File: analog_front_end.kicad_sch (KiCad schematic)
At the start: 14 parts, among them J3 Conn_01x03_Pin, J4 Conn_01x03_Pin, Q3 BC847,215, Q4 BSS316N, U7 OPA388IDBV

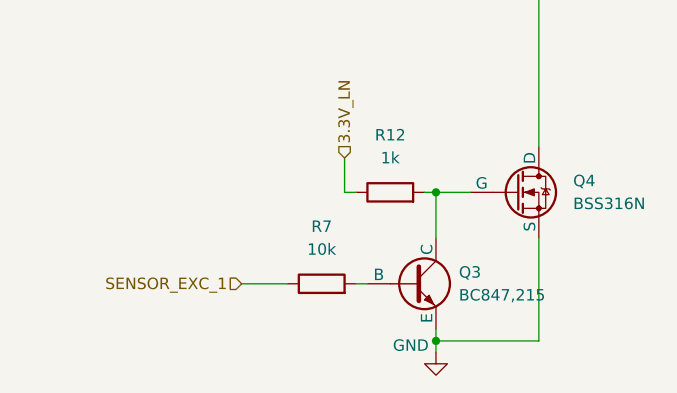
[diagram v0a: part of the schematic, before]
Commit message: rule-check: Fix the ERC errors and warnings
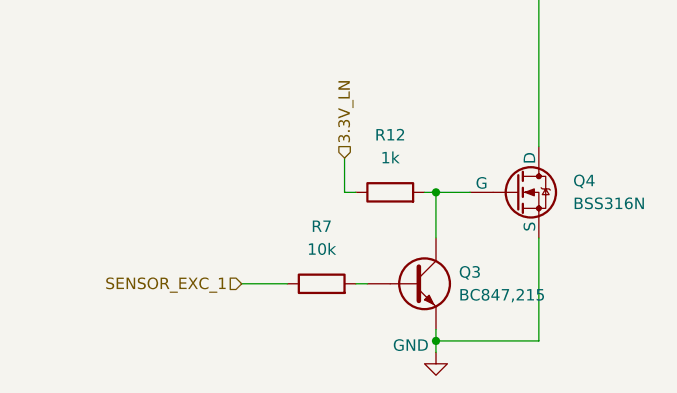
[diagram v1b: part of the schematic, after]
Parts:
- Q3: symbol Simulation_SPICE:NPN -> Device:Q_NPN
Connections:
- net GND: now also Q3.E; no longer Q3.3 (E)
- net at R7.2: now also Q3.B; no longer Q3.2 (B)
- net at Q4.2 (G), R12.2: now also Q3.C; no longer Q3.1 (C)
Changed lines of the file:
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@@
+			)
+		)
+		(property "LCSC" ""
+			(at 86.36 111.76 0)
+			(effects
+				(font
+					(size 1.27 1.27)
+				)
+				(hide yes)
 			)
 		)
@@
 	)
 	(symbol
-		(lib_id "Simulation_SPICE:NPN")
+		(lib_id "Device:Q_NPN")
 		(at 193.04 140.97 0)
 		(unit 1)
@@
 			)
 		)
-		(pin "2"
-		)
-		(pin "1"
-		)
-		(pin "3"
-		)
-		(instances
+		(property "LCSC" ""
+			(at 193.04 140.97 0)
+			(effects
+				(font
+					(size 1.27 1.27)
+				)
+				(hide yes)
+			)
+		)
+		(pin "C"
+		)
+		(pin "B"
+		)
+		(pin "E"
+		)
+		(instances

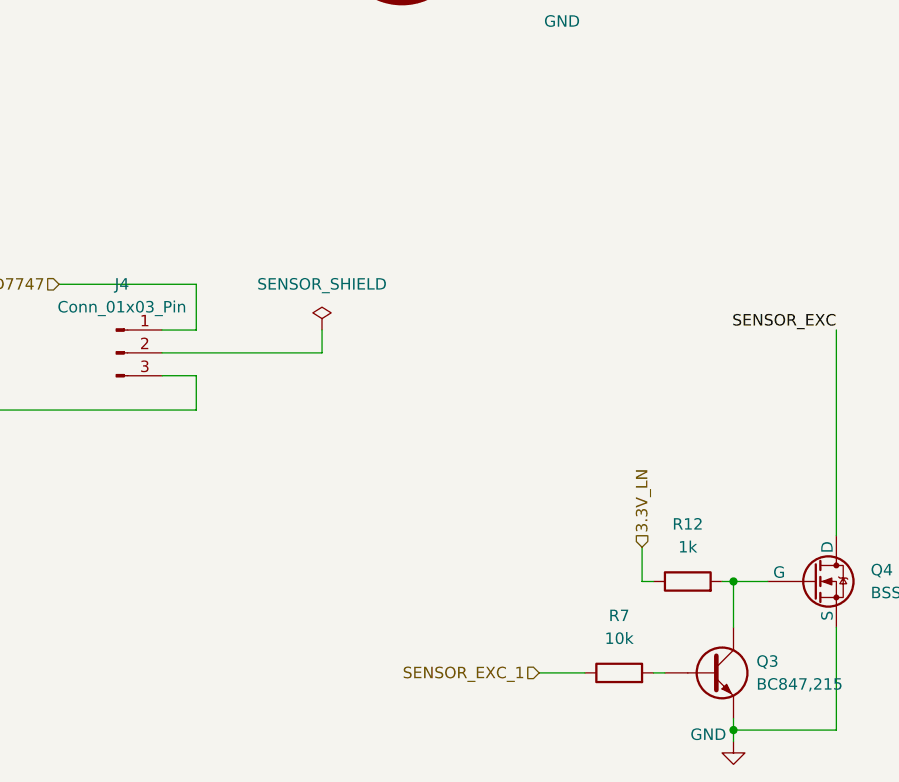
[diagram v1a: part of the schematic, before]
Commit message: design: fix some rules check
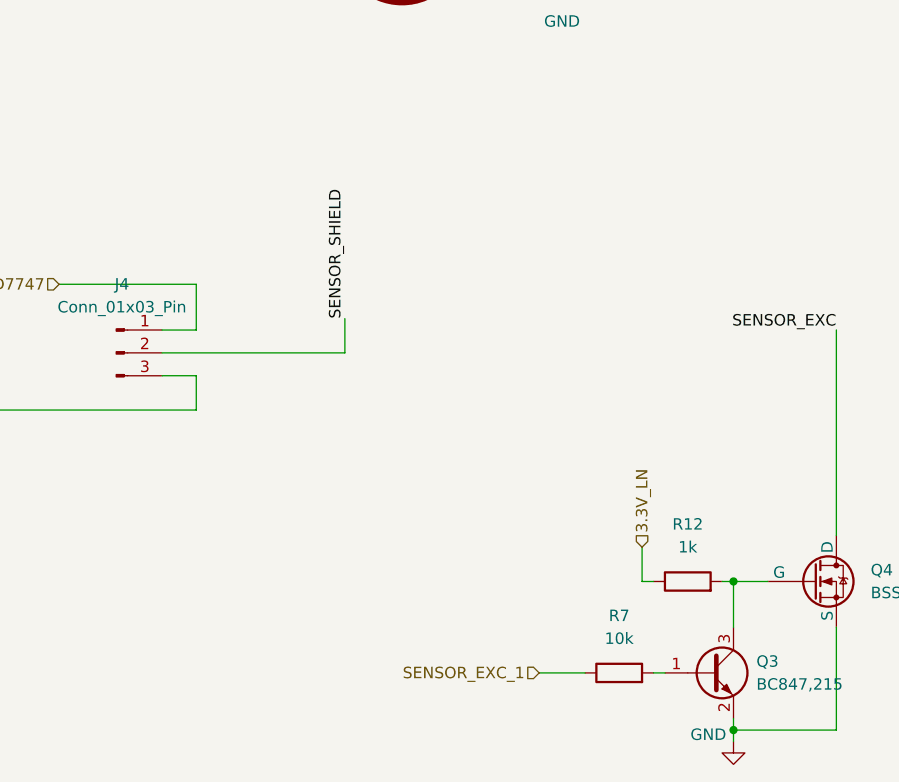
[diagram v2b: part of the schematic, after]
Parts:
- Q3: symbol Device:Q_NPN -> Transistor_BJT:BC847
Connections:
- net GND: now also Q3.2 (E); no longer Q3.E
- net at R7.2: now also Q3.1 (B); no longer Q3.B
- net at Q4.2 (G), R12.2: now also Q3.3 (C); no longer Q3.C
- net SENSOR_SHIELD: now reaches J4.2 (Pin_2)
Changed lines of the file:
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@@
 	(wire
 		(pts
-			(xy 149.86 102.87) (xy 149.86 105.41)
+			(xy 152.4 101.6) (xy 152.4 105.41)
 		)
 		(stroke
@@
 	(wire
 		(pts
-			(xy 132.08 105.41) (xy 149.86 105.41)
+			(xy 132.08 105.41) (xy 152.4 105.41)
 		)
 		(stroke
@@
 			(width 0)
 			(type default)
+		)
+	)
+	(label "SENSOR_SHIELD"
+		(at 152.4 101.6 90)
+		(effects
+			(font
+				(size 1.27 1.27)
+			)
+			(justify left bottom)
 		)
 	)
@@
 	)
 	(symbol
-		(lib_id "power:PWR_FLAG")
-		(at 149.86 102.87 0)
-		(unit 1)
-		(exclude_from_sim no)
-		(in_bom yes)
-		(on_board yes)
-		(dnp no)
-		(fields_autoplaced yes)
-		(property "Reference" "#FLG01"
-			(at 149.86 100.965 0)
-			(effects
-				(font
-					(size 1.27 1.27)
-				)
-				(hide yes)
-			)
-		)
-		(property "Value" "SENSOR_SHIELD"
-			(at 149.86 97.79 0)
-			(effects
-				(font
-					(size 1.27 1.27)
-				)
-			)
-		)
-		(property "Footprint" ""
-			(at 149.86 102.87 0)
-			(effects
-				(font
-					(size 1.27 1.27)
-				)
-				(hide yes)
-			)
-		)
-		(property "Datasheet" "~"
-			(at 149.86 102.87 0)
-			(effects
-				(font
-					(size 1.27 1.27)
-				)
-				(hide yes)
-			)
-		)
-		(property "Description" "Special symbol for telling ERC where power comes from"
-			(at 149.86 102.87 0)
-			(effects
-				(font
-					(size 1.27 1.27)
-				)
-				(hide yes)
-			)
-		)
-		(pin "1"
-		)
-		(instances
-			(project ""
-				(path "/dedd74c5-8e82-403a-8a1b-f763d3ee00bb/2a3fb7ae-12df-4167-9b5f-4fb9d4c182aa"
-					(reference "#FLG01")
-					(unit 1)
-				)
-			)
-		)
-	)
-	(symbol
 		(lib_id "Connector:Conn_01x03_Pin")
 		(at 115.57 59.69 0)
@@
 	)
 	(symbol
-		(lib_id "Device:Q_NPN")
+		(lib_id "Transistor_BJT:BC847")
 		(at 193.04 140.97 0)
 		(unit 1)
@@
 		)
 		(property "Footprint" "Package_TO_SOT_SMD:SOT-23"
-			(at 256.54 140.97 0)
-			(effects
-				(font
-					(size 1.27 1.27)
-				)
-				(hide yes)
-			)
-		)
-		(property "Datasheet" "https://ngspice.sourceforge.io/docs/ngspice-html-manual/manual.xhtml#cha_BJTs"
-			(at 256.54 140.97 0)
-			(effects
-				(font
-					(size 1.27 1.27)
-				)
-				(hide yes)
-			)
-		)
-		(property "Description" "Bipolar transistor symbol for simulation only, substrate tied to the emitter"
+			(at 198.12 142.875 0)
+			(effects
+				(font
+					(size 1.27 1.27)
+					(italic yes)
+				)
+				(justify left)
+				(hide yes)
+			)
+		)
+		(property "Datasheet" "http://www.infineon.com/dgdl/Infineon-BC847SERIES_BC848SERIES_BC849SERIES_BC850SERIES-DS-v01_01-en.pdf?fileId=db3a304314dca389011541d4630a1657"
+			(at 193.04 140.97 0)
+			(effects
+				(font
+					(size 1.27 1.27)
+				)
+				(justify left)
+				(hide yes)
+			)
+		)
+		(property "Description" "0.1A Ic, 45V Vce, NPN Transistor, SOT-23"
 			(at 193.04 140.97 0)
 			(effects
@@
 			)
 		)
-		(property "Sim.Pins" "1=C 2=B 3=E"
+		(property "Sim.Pins" "C=C B=B E=E"
 			(at 193.04 140.97 0)
 			(effects
@@
 			)
 		)
-		(pin "C"
-		)
-		(pin "B"
-		)
-		(pin "E"
+		(pin "3"
+		)
+		(pin "1"
+		)
+		(pin "2"
 		)
 		(instances

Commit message: design: fix some erc/drc
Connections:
- net SENSOR_EXCITATION: now reaches E1.1 (+), J3.2 (Pin_2)
- net SENSOR_EXC renamed SENSOR_EXC_MCU
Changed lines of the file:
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@@
 		)
 	)
-	(label "SENSOR_EXC"
+	(label "SENSOR_EXC_MCU"
 		(at 73.66 106.68 90)
 		(effects
@@
 		)
 	)
-	(label "SENSOR_EXC"
+	(label "SENSOR_EXC_MCU"
 		(at 104.14 64.77 180)
 		(effects
@@
 		)
 	)
-	(label "SENSOR_EXC"
+	(label "SENSOR_EXCITATION"
+		(at 128.27 59.69 0)
+		(effects
+			(font
+				(size 1.27 1.27)
+			)
+			(justify left bottom)
+		)
+	)
+	(label "SENSOR_EXC_MCU"
 		(at 207.01 102.87 180)
 		(effects
@@
 			(at 158.75 59.69 0)
 			(effects
+				(font
+					(size 1.27 1.27)
+				)
+				(hide yes)
+			)
+		)
+		(property "LCSC" ""
+			(at 158.75 59.69 0)
+			(effects

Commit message: chore: fix the naming of connectors sheet file name and the change the path of footprints
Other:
- title: (none) -> ${SHEETNAME}
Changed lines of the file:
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@@
 	(generator_version "9.0")
 	(paper "A4")
+	(title_block
+		(title "${SHEETNAME}")
+	)
 	(text "Keep close to U7\n\n\n\n"
 		(exclude_from_sim no)

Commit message: chore: update project to use local footprint and symbols
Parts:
- C12, C17: footprint Capacitor_SMD:C_0603_1608Metric -> footprints:C_0603_1608Metric; symbol Device:C -> symbols:C
- E1: footprint el-ce:CapacitiveElectrode-round_20mmx70mm -> footprints:CapacitiveElectrode-round_20mmx70mm; symbol el_ce-misc:CapacitiveElectrode-2_electrodes -> symbols:CapacitiveElectrode-2_electrodes
- J3, J4: footprint Connector_PinHeader_2.54mm:PinHeader_1x03_P2.54mm_Vertical -> footprints:PinHeader_1x03_P2.54mm_Vertical; symbol Connector:Conn_01x03_Pin -> symbols:Conn_01x03_Pin
- Q3: footprint Package_TO_SOT_SMD:SOT-23 -> footprints:SOT-23; symbol Transistor_BJT:BC847 -> symbols:BC847
- Q4: footprint Package_TO_SOT_SMD:SOT-23 -> footprints:SOT-23; symbol Simulation_SPICE:NMOS -> symbols:NMOS
- R10, R11, R12, R7, R8, R9: footprint Resistor_SMD:R_0603_1608Metric -> footprints:R_0603_1608Metric; symbol Device:R -> symbols:R
- U7: footprint Package_TO_SOT_SMD:SOT-23-5 -> footprints:SOT-23-5; symbol Simulation_SPICE:OPAMP -> symbols:OPAMP
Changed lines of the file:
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@@
 	)
 	(symbol
-		(lib_id "power:GND")
+		(lib_id "symbols:GND")
 		(at 195.58 148.59 0)
 		(unit 1)
@@
 	)
 	(symbol
-		(lib_id "Simulation_SPICE:OPAMP")
+		(lib_id "symbols:OPAMP")
 		(at 86.36 111.76 0)
 		(unit 1)
@@
 			)
 		)
-		(property "Footprint" "Package_TO_SOT_SMD:SOT-23-5"
+		(property "Footprint" "footprints:SOT-23-5"
 			(at 86.36 111.76 0)
 			(effects
@@
 			)
 		)
-		(property "Datasheet" "https://www.ti.com/lit/ds/symlink/opa388.pdf"
+		(property "Datasheet" ""
 			(at 86.36 111.76 0)
 			(effects
@@
 			)
 		)
-		(property "Description" "Operational amplifier, single"
+		(property "Description" ""
 			(at 86.36 111.76 0)
 			(effects
@@
 			)
 		)
-		(property "Sim.Pins" "1=in+ 2=in- 3=vcc 4=vee 5=out"
-			(at 86.36 111.76 0)
-			(effects
-				(font
-					(size 1.27 1.27)
-				)
-				(hide yes)
-			)
-		)
-		(property "Sim.Device" "SUBCKT"
-			(at 86.36 111.76 0)
-			(effects
-				(font
-					(size 1.27 1.27)
-				)
-				(justify left)
-				(hide yes)
-			)
-		)
-		(property "Sim.Library" "${KICAD8_SYMBOL_DIR}/Simulation_SPICE.sp"
-			(at 86.36 111.76 0)
-			(effects
-				(font
-					(size 1.27 1.27)
-				)
-				(hide yes)
-			)
-		)
-		(property "Sim.Name" "kicad_builtin_opamp"
-			(at 86.36 111.76 0)
-			(effects
-				(font
-					(size 1.27 1.27)
-				)
-				(hide yes)
-			)
-		)
-		(property "LCSC" ""
-			(at 86.36 111.76 0)
-			(effects
-				(font
-					(size 1.27 1.27)
-				)
-				(hide yes)
-			)
-		)
 		(pin "3"
 		)
@@
 	)
 	(symbol
-		(lib_id "power:GND")
+		(lib_id "symbols:GND")
 		(at 16.51 40.64 0)
 		(unit 1)
@@
 	)
 	(symbol
-		(lib_id "Device:R")
+		(lib_id "symbols:R")
 		(at 182.88 140.97 90)
 		(unit 1)
@@
 			)
 		)
-		(property "Footprint" "Resistor_SMD:R_0603_1608Metric"
+		(property "Footprint" "footprints:R_0603_1608Metric"
 			(at 182.88 142.748 90)
 			(effects
@@
 	)
 	(symbol
-		(lib_id "Device:R")
+		(lib_id "symbols:R")
 		(at 59.69 113.03 90)
 		(unit 1)
@@
 			)
 		)
-		(property "Footprint" "Resistor_SMD:R_0603_1608Metric"
+		(property "Footprint" "footprints:R_0603_1608Metric"
 			(at 59.69 114.808 90)
 			(effects
@@
 	)
 	(symbol
-		(lib_id "Device:R")
+		(lib_id "symbols:R")
 		(at 59.69 104.14 90)
 		(unit 1)
@@
 			)
 		)
-		(property "Footprint" "Resistor_SMD:R_0603_1608Metric"
+		(property "Footprint" "footprints:R_0603_1608Metric"
 			(at 59.69 105.918 90)
 			(effects
@@
 	)
 	(symbol
-		(lib_id "Device:R")
+		(lib_id "symbols:R")
 		(at 190.5 130.81 90)
 		(unit 1)
@@
 			)
 		)
-		(property "Footprint" "Resistor_SMD:R_0603_1608Metric"
+		(property "Footprint" "footprints:R_0603_1608Metric"
 			(at 190.5 132.588 90)
 			(effects
@@
 	)
 	(symbol
-		(lib_id "Simulation_SPICE:NMOS")
+		(lib_id "symbols:NMOS")
 		(at 204.47 130.81 0)
 		(unit 1)
@@
 			)
 		)
-		(property "Footprint" "Package_TO_SOT_SMD:SOT-23"
+		(property "Footprint" "footprints:SOT-23"
 			(at 209.55 128.27 0)
 			(effects
@@
 	)
 	(symbol
-		(lib_id "Connector:Conn_01x03_Pin")
+		(lib_id "symbols:Conn_01x03_Pin")
 		(at 115.57 59.69 0)
 		(unit 1)
@@
 			)
 		)
-		(property "Footprint" "Connector_PinHeader_2.54mm:PinHeader_1x03_P2.54mm_Vertical"
+		(property "Footprint" "footprints:PinHeader_1x03_P2.54mm_Vertical"
 			(at 115.57 59.69 0)
 			(effects
@@
 	)
 	(symbol
-		(lib_id "Transistor_BJT:BC847")
+		(lib_id "symbols:BC847")
 		(at 193.04 140.97 0)
 		(unit 1)
@@
 			)
 		)
-		(property "Footprint" "Package_TO_SOT_SMD:SOT-23"
+		(property "Footprint" "footprints:SOT-23"
 			(at 198.12 142.875 0)
 			(effects
@@
 	)
 	(symbol
-		(lib_id "Connector:Conn_01x03_Pin")
+		(lib_id "symbols:Conn_01x03_Pin")
 		(at 127 105.41 0)
 		(unit 1)
@@
 			)
 		)
-		(property "Footprint" "Connector_PinHeader_2.54mm:PinHeader_1x03_P2.54mm_Vertical"
+		(property "Footprint" "footprints:PinHeader_1x03_P2.54mm_Vertical"
 			(at 127 105.41 0)
 			(effects
@@
 	)
 	(symbol
-		(lib_id "Device:R")
+		(lib_id "symbols:R")
 		(at 59.69 95.25 90)
 		(unit 1)
@@
 			)
 		)
-		(property "Footprint" "Resistor_SMD:R_0603_1608Metric"
+		(property "Footprint" "footprints:R_0603_1608Metric"
 			(at 59.69 97.028 90)
 			(effects
@@
 	)
 	(symbol
-		(lib_id "Device:R")
+		(lib_id "symbols:R")
 		(at 59.69 121.92 90)
 		(unit 1)
@@
 			)
 		)
-		(property "Footprint" "Resistor_SMD:R_0603_1608Metric"
+		(property "Footprint" "footprints:R_0603_1608Metric"
 			(at 59.69 123.698 90)
 			(effects
@@
 	)
 	(symbol
-		(lib_id "power:GND")
+		(lib_id "symbols:GND")
 		(at 176.53 63.5 0)
 		(unit 1)
@@
 	)
 	(symbol
-		(lib_id "Device:C")
+		(lib_id "symbols:C")
 		(at 29.21 31.75 0)
 		(unit 1)
@@
 			)
 		)
-		(property "Footprint" "Capacitor_SMD:C_0603_1608Metric"
+		(property "Footprint" "footprints:C_0603_1608Metric"
 			(at 30.1752 35.56 0)
 			(effects
@@
 	)
 	(symbol
-		(lib_id "Device:C")
+		(lib_id "symbols:C")
 		(at 16.51 31.75 0)
 		(unit 1)
@@
 			)
 		)
-		(property "Footprint" "Capacitor_SMD:C_0603_1608Metric"
+		(property "Footprint" "footprints:C_0603_1608Metric"
 			(at 17.4752 35.56 0)
 			(effects
@@
 	)
 	(symbol
-		(lib_id "el_ce-misc:CapacitiveElectrode-2_electrodes")
+		(lib_id "symbols:CapacitiveElectrode-2_electrodes")
 		(at 158.75 59.69 0)
 		(unit 1)
@@
 			)
 		)
-		(property "Footprint" "el-ce:CapacitiveElectrode-round_20mmx70mm"
+		(property "Footprint" "footprints:CapacitiveElectrode-round_20mmx70mm"
 			(at 158.75 59.69 0)
 			(effects
@@
 			)
 		)
-		(property "LCSC" ""
-			(at 158.75 59.69 0)
-			(effects
-				(font
-					(size 1.27 1.27)
-				)
-				(hide yes)
-			)
-		)
 		(pin "1"
 		)
@@
 	)
 	(symbol
-		(lib_id "power:GND")
+		(lib_id "symbols:GND")
 		(at 83.82 120.65 0)
 		(unit 1)

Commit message: design: change mosfet simulation model to use a generic model and useless remove erc exclusion
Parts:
- U7: footprint footprints:SOT-23-5 -> Package_TO_SOT_SMD:SOT-23-5
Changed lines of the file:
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@@
 		(fields_autoplaced yes)
 		(property "Reference" "U7"
-			(at 93.98 106.7114 0)
+			(at 99.06 105.3398 0)
 			(effects
 				(font
@@
 		)
 		(property "Value" "OPA388IDBV"
-			(at 93.98 108.6165 0)
-			(effects
-				(font
-					(size 1.27 1.27)
-				)
-			)
-		)
-		(property "Footprint" "footprints:SOT-23-5"
-			(at 86.36 111.76 0)
-			(effects
-				(font
-					(size 1.27 1.27)
-				)
-				(hide yes)
-			)
-		)
-		(property "Datasheet" ""
-			(at 86.36 111.76 0)
-			(effects
-				(font
-					(size 1.27 1.27)
-				)
-				(hide yes)
-			)
-		)
-		(property "Description" ""
+			(at 99.06 107.8798 0)
+			(effects
+				(font
+					(size 1.27 1.27)
+				)
+			)
+		)
+		(property "Footprint" "Package_TO_SOT_SMD:SOT-23-5"
+			(at 86.36 111.76 0)
+			(effects
+				(font
+					(size 1.27 1.27)
+				)
+				(hide yes)
+			)
+		)
+		(property "Datasheet" "https://ngspice.sourceforge.io/docs/ngspice-html-manual/manual.xhtml#sec__SUBCKT_Subcircuits"
+			(at 86.36 111.76 0)
+			(effects
+				(font
+					(size 1.27 1.27)
+				)
+				(hide yes)
+			)
+		)
+		(property "Description" "Operational amplifier, single"
+			(at 86.36 111.76 0)
+			(effects
+				(font
+					(size 1.27 1.27)
+				)
+				(hide yes)
+			)
+		)
+		(property "Sim.Pins" "1=in+ 2=in- 3=vcc 4=vee 5=out"
+			(at 86.36 111.76 0)
+			(effects
+				(font
+					(size 1.27 1.27)
+				)
+				(hide yes)
+			)
+		)
+		(property "Sim.Device" "SUBCKT"
+			(at 86.36 111.76 0)
+			(effects
+				(font
+					(size 1.27 1.27)
+				)
+				(justify left)
+				(hide yes)
+			)
+		)
+		(property "Sim.Library" "${KICAD8_SYMBOL_DIR}/Simulation_SPICE.sp"
+			(at 86.36 111.76 0)
+			(effects
+				(font
+					(size 1.27 1.27)
+				)
+				(hide yes)
+			)
+		)
+		(property "Sim.Name" "kicad_builtin_opamp"
 			(at 86.36 111.76 0)
 			(effects
@@
 			)
 		)
-		(property "Sim.Device" "SUBCKT"
+		(property "Sim.Device" "NMOS"
 			(at 204.47 147.955 0)
 			(effects
@@
 			)
 		)
-		(property "Sim.Pins" "1=10 2=20 3=30"
+		(property "Sim.Pins" "1=D 2=G 3=S"
 			(at 204.47 146.05 0)
 			(effects
@@
 			)
 		)
-		(property "Sim.Library" "/tools/kicad/spice/2N7002.spice.txt"
+		(property "LCSC" ""
 			(at 204.47 130.81 0)
 			(effects
@@
 			)
 		)
-		(property "Sim.Name" "N7002"
+		(property "Sim.Type" "VDMOS"
 			(at 204.47 130.81 0)
 			(effects
